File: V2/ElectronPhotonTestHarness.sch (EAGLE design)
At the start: 43 parts, among them IC1 7805TV, Q1 200mA/50V, Q2 200mA/50V, U1 ELECTRONDUALNAMED, U2 UnderTest

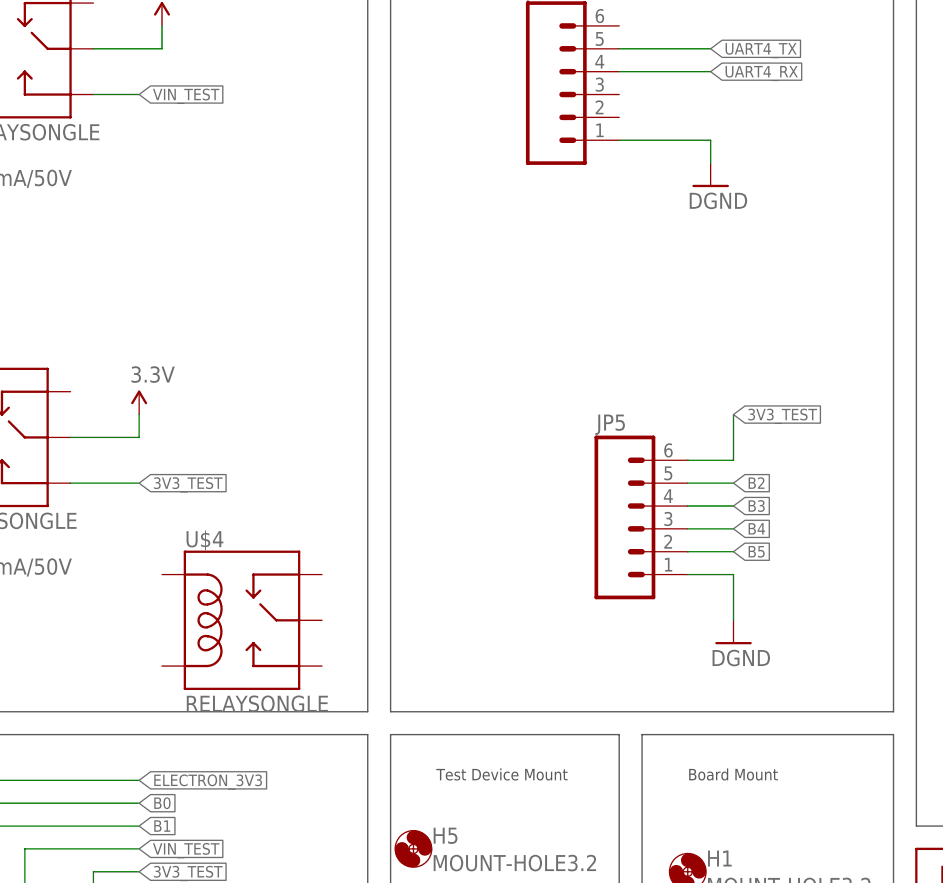
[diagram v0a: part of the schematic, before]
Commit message: Tidy up for main test harness board.
Made test top (well middle) board for Pogo pins to rest in.
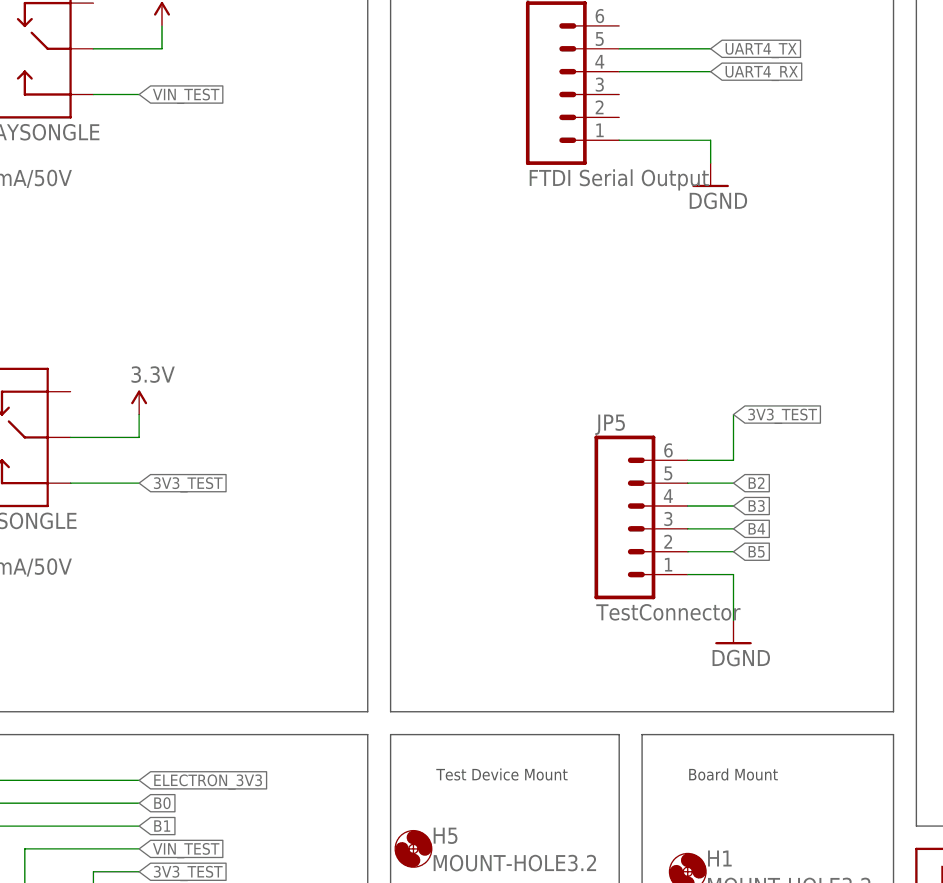
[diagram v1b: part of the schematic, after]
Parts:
- removed U$4: RELAYSONGLE, Particle:RELAYSONGLE
- JP4: value (none) -> FTDI Serial Output
- JP5: value (none) -> TestConnector
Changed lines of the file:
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@@
 <part name="SUPPLY1" library="SparkFun-Aesthetics" deviceset="5V" device=""/>
 <part name="GND17" library="SparkFun-Aesthetics" deviceset="DGND" device=""/>
-<part name="JP4" library="SparkFun-Connectors" deviceset="M06" device="SILK_FEMALE_PTH"/>
-<part name="JP5" library="SparkFun-Connectors" deviceset="M06" device="SILK_FEMALE_PTH"/>
+<part name="JP4" library="SparkFun-Connectors" deviceset="M06" device="SILK_FEMALE_PTH" value="FTDI Serial Output"/>
+<part name="JP5" library="SparkFun-Connectors" deviceset="M06" device="SILK_FEMALE_PTH" value="TestConnector"/>
 <part name="GND18" library="SparkFun-Aesthetics" deviceset="DGND" device=""/>
 <part name="C1" library="SparkFun-Capacitors" deviceset="1.0UF-25V-+80/-20(0805)" device="&quot;" value="1.0uF"/>
@@
 <part name="TP3" library="testpad" deviceset="TP" device="TP12SQ"/>
 <part name="U$3" library="Particle" deviceset="RELAY" device="SONGLE"/>
-<part name="U$4" library="Particle" deviceset="RELAY" device="SONGLE"/>
 </parts>
 <sheets>
@@
 <instance part="TP3" gate="G$1" x="66.04" y="68.58" rot="R180"/>
 <instance part="U$3" gate="G$1" x="-7.62" y="33.02"/>
-<instance part="U$4" gate="G$1" x="17.78" y="-30.48"/>
 </instances>
 <busses>
